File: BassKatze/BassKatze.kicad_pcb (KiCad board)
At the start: 2 copper layers, 55 x 54.9 mm, 55 parts, among them J1 Conn_01x02_Female, Q1 IRF7404, Q2 BSS138, Q3 BSS138, Q4 BSS138, Q5 BSS138, Q6 BSS138, SW1 SW_Push, U1 ATmega328-AU, U2 MSGEQ7, U3 TP4056

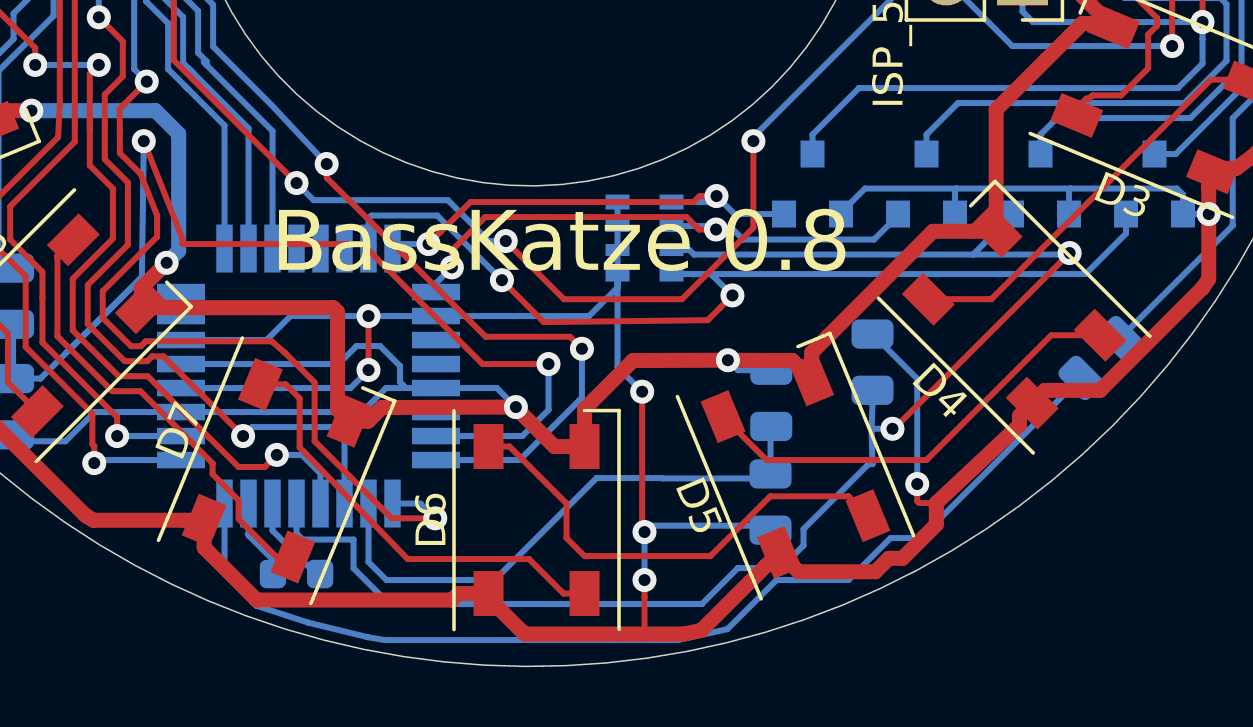
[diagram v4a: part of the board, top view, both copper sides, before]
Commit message: basskatze 0.9 -> removed redundant reset pullup
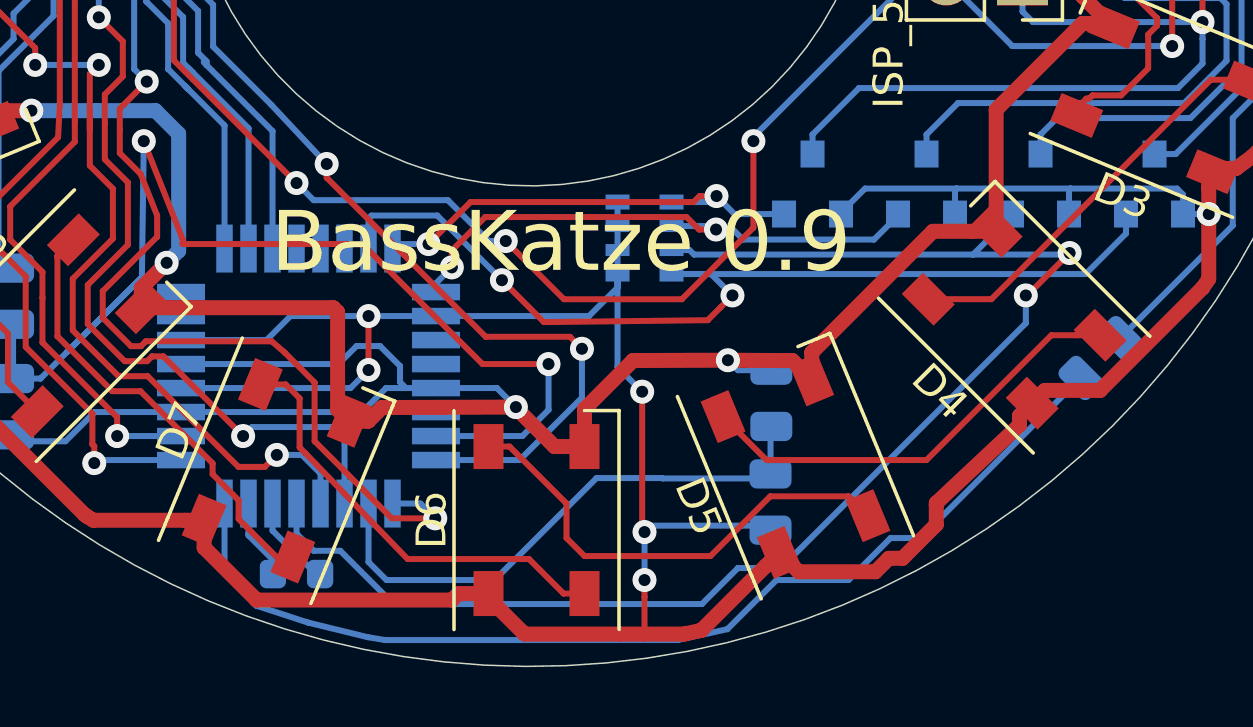
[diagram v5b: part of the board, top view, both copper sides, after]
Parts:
- removed R5: 10KOhm, Resistor_SMD:R_0805_2012Metric
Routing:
- net PWR: track 282.6 -> 275.8 mm, vias 14 -> 13
- net Reset: track 50.7 -> 48.4 mm
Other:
- board text added: "BassKatze 0.9"
- board text removed: "BassKatze 0.8"
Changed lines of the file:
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@@
     (thickness 1.6)
     (drawings 5)
-    (tracks 1097)
+    (tracks 1084)
     (zones 0)
-    (modules 55)
+    (modules 54)
     (nets 56)
   )
@@
     )
   )
-  (module Resistor_SMD:R_0805_2012Metric (layer B.Cu)
-    (at 138.4 144.3375 90)
-    (descr "Resistor SMD 0805 (2012 Metric), square (rectangular) end terminal, IPC_7351 nominal, (Body size source: https://docs.google.com/spreadsheets/d/1BsfQQcO9C6DZCsRaXUlFlo91Tg2WpOkGARC1WS5S8t0/edit?usp=sharing), generated with kicad-footprint-generator")
-    (tags resistor)
-    (attr smd)
-    (fp_text reference R5 (at 0 1.65 90) (layer B.SilkS)
-      (effects (font (size 1 1) (thickness 0.15)) (justify mirror))
-    )
-    (fp_text value 10KOhm (at 0 -1.65 90) (layer B.Fab)
-      (effects (font (size 1 1) (thickness 0.15)) (justify mirror))
-    )
-    (fp_line (start -1 -0.6) (end -1 0.6) (layer B.Fab) (width 0.1))
-    (fp_line (start -1 0.6) (end 1 0.6) (layer B.Fab) (width 0.1))
-    (fp_line (start 1 0.6) (end 1 -0.6) (layer B.Fab) (width 0.1))
-    (fp_line (start 1 -0.6) (end -1 -0.6) (layer B.Fab) (width 0.1))
-    (fp_line (start -0.258578 0.71) (end 0.258578 0.71) (layer B.SilkS) (width 0.12))
-    (fp_line (start -0.258578 -0.71) (end 0.258578 -0.71) (layer B.SilkS) (width 0.12))
-    (fp_line (start -1.68 -0.95) (end -1.68 0.95) (layer B.CrtYd) (width 0.05))
-    (fp_line (start -1.68 0.95) (end 1.68 0.95) (layer B.CrtYd) (width 0.05))
-    (fp_line (start 1.68 0.95) (end 1.68 -0.95) (layer B.CrtYd) (width 0.05))
-    (fp_line (start 1.68 -0.95) (end -1.68 -0.95) (layer B.CrtYd) (width 0.05))
-    (fp_text user %R (at 0 0 90) (layer B.Fab)
-      (effects (font (size 0.5 0.5) (thickness 0.08)) (justify mirror))
-    )
-    (pad 1 smd roundrect (at -0.9375 0 90) (size 0.975 1.4) (layers B.Cu B.Paste B.Mask) (roundrect_rratio 0.25)
-      (net 10 Reset))
-    (pad 2 smd roundrect (at 0.9375 0 90) (size 0.975 1.4) (layers B.Cu B.Paste B.Mask) (roundrect_rratio 0.25)
-      (net 7 PWR))
-    (model ${KISYS3DMOD}/Resistor_SMD.3dshapes/R_0805_2012Metric.wrl
-      (at (xyz 0 0 0))
-      (scale (xyz 1 1 1))
-      (rotate (xyz 0 0 0))
-    )
-  )
   (module Resistor_SMD:R_1206_3216Metric_Pad1.42x1.75mm_HandSolder (layer B.Cu)
     (at 127.8255 112.8395 90)
@@
     )
   )
-  (gr_text "BassKatze 0.8" (at 128.016 140.335) (layer F.SilkS)
+  (gr_text "BassKatze 0.9" (at 128.016 140.335) (layer F.SilkS)
     (effects (font (size 2 2) (thickness 0.15)))
   )
@@
   (segment (start 147.1 114.895) (end 147.609654 114.895) (width 0.5) (layer B.Cu) (net 7))
   (via (at 149.2 113.304654) (size 0.8) (drill 0.4) (layers F.Cu B.Cu) (net 7))
-  (via (at 139.889844 148.4) (size 0.8) (drill 0.4) (layers F.Cu B.Cu) (net 7))
-  (segment (start 138.4 143.4) (end 139.889844 144.889844) (width 0.2) (layer B.Cu) (net 7))
-  (segment (start 139.889844 144.889844) (end 139.889844 148.4) (width 0.2) (layer B.Cu) (net 7))
-  (segment (start 139.889844 148.965685) (end 139.958659 149.0345) (width 0.2) (layer F.Cu) (net 7))
-  (segment (start 139.889844 148.4) (end 139.889844 148.965685) (width 0.2) (layer F.Cu) (net 7))
-  (segment (start 139.958659 149.0345) (end 140.5255 149.0345) (width 0.2) (layer F.Cu) (net 7))
   (segment (start 140.5255 149.0345) (end 143.298813 146.433095) (width 0.5) (layer F.Cu) (net 7))
   (segment (start 101.95 125.6) (end 101.7 125.6) (width 0.5) (layer F.Cu) (net 7))
@@
   (segment (start 133.331001 142.512999) (end 132.9055 142.9385) (width 0.2) (layer F.Cu) (net 9))
   (segment (start 127.4445 143.002) (end 132.9055 142.9385) (width 0.2) (layer F.Cu) (net 9))
-  (segment (start 107.315 123.444) (end 107.188 123.571) (width 0.2) (layer B.Cu) (net 17))
-  (segment (start 138.4 145.7625) (end 138.4 145.275) (width 0.2) (layer B.Cu) (net 10))
-  (segment (start 122.292881 152.400001) (end 132.712459 152.400001) (width 0.2) (layer B.Cu) (net 10))
-  (segment (start 121.09999 151.20711) (end 122.292881 152.400001) (width 0.2) (layer B.Cu) (net 10))
-  (segment (start 121.09999 150.250001) (end 121.09999 151.20711) (width 0.2) (layer B.Cu) (net 10))
-  (segment (start 119.404999 150.250001) (end 121.09999 150.250001) (width 0.2) (layer B.Cu) (net 10))
-  (segment (start 119.2 150.045002) (end 119.404999 150.250001) (width 0.2) (layer B.Cu) (net 10))
-  (segment (start 119.2 149.05) (end 119.2 150.045002) (width 0.2) (layer B.Cu) (net 10))
   (segment (start 132.3 140.6) (end 131.7 140.6) (width 0.2) (layer B.Cu) (net 10))
   (segment (start 132.450011 140.750011) (end 132.3 140.6) (width 0.2) (layer B.Cu) (net 10))
@@
   (segment (start 143.05 139.45) (end 141.749989 140.750011) (width 0.2) (layer B.Cu) (net 10))
   (segment (start 143.05 139.4) (end 143.05 139.45) (width 0.2) (layer B.Cu) (net 10))
+  (segment (start 144.920489 140.750011) (end 144.9705 140.7) (width 0.2) (layer B.Cu) (net 10))
+  (segment (start 141.749989 140.750011) (end 144.920489 140.750011) (width 0.2) (layer B.Cu) (net 10))
   (via (at 144.9705 140.7) (size 0.8) (drill 0.4) (layers F.Cu B.Cu) (net 10))
-  (segment (start 141.749989 140.750011) (end 144.920489 140.750011) (width 0.2) (layer B.Cu) (net 10))
-  (segment (start 144.920489 140.750011) (end 144.9705 140.7) (width 0.2) (layer B.Cu) (net 10))
-  (via (at 139.065 146.558) (size 0.8) (drill 0.4) (layers F.Cu B.Cu) (net 10))
-  (segment (start 144.9705 140.7) (end 139.1125 146.558) (width 0.2) (layer F.Cu) (net 10))
-  (segment (start 139.1125 146.558) (end 139.065 146.558) (width 0.2) (layer F.Cu) (net 10))
-  (segment (start 138.4 147.73756) (end 138.3665 146.558) (width 0.2) (layer B.Cu) (net 10))
-  (segment (start 139.065 146.558) (end 138.3665 146.558) (width 0.2) (layer B.Cu) (net 10))
-  (segment (start 138.3665 146.558) (end 138.4 145.7625) (width 0.2) (layer B.Cu) (net 10))
-  (segment (start 136.10001 150.447906) (end 135.347926 151.19999) (width 0.2) (layer B.Cu) (net 10))
-  (segment (start 133.91247 151.19999) (end 132.712459 152.400001) (width 0.2) (layer B.Cu) (net 10))
-  (segment (start 135.347926 151.19999) (end 133.91247 151.19999) (width 0.2) (layer B.Cu) (net 10))
-  (segment (start 136.10001 149.90399) (end 136.10001 150.447906) (width 0.2) (layer B.Cu) (net 10))
-  (segment (start 138.26644 147.73756) (end 136.10001 149.90399) (width 0.2) (layer B.Cu) (net 10))
-  (segment (start 138.4 147.73756) (end 138.26644 147.73756) (width 0.2) (layer B.Cu) (net 10))
+  (via (at 143.51 142.113) (size 0.8) (drill 0.4) (layers F.Cu B.Cu) (net 10))
+  (segment (start 144.9705 140.7) (end 143.5575 142.113) (width 0.2) (layer F.Cu) (net 10))
+  (segment (start 143.5575 142.113) (end 143.51 142.113) (width 0.2) (layer F.Cu) (net 10))
+  (segment (start 143.51 143.037916) (end 143.51 142.113) (width 0.2) (layer B.Cu) (net 10))
+  (segment (start 135.347926 151.19999) (end 143.51 143.037916) (width 0.2) (layer B.Cu) (net 10))
+  (segment (start 133.91247 151.19999) (end 135.347926 151.19999) (width 0.2) (layer B.Cu) (net 10))
+  (segment (start 132.712459 152.400001) (end 133.91247 151.19999) (width 0.2) (layer B.Cu) (net 10))
+  (segment (start 122.434302 152.4) (end 132.712459 152.400001) (width 0.2) (layer B.Cu) (net 10))
+  (segment (start 119.77499 150.62499) (end 120.659292 150.62499) (width 0.2) (layer B.Cu) (net 10))
+  (segment (start 120.659292 150.62499) (end 122.434302 152.4) (width 0.2) (layer B.Cu) (net 10))
+  (segment (start 119.2 150.05) (end 119.77499 150.62499) (width 0.2) (layer B.Cu) (net 10))
+  (segment (start 119.2 149.05) (end 119.2 150.05) (width 0.2) (layer B.Cu) (net 10))
   (via (at 133.184316 139.915687) (size 0.8) (drill 0.4) (layers F.Cu B.Cu) (net 11))
   (segment (start 131.7 139.8) (end 133.068629 139.8) (width 0.2) (layer B.Cu) (net 11))
@@
   (segment (start 112.609469 131.377906) (end 112.609469 132.842) (width 0.2) (layer B.Cu) (net 16))
   (segment (start 109.601 123.6345) (end 109.6645 127.8255) (width 0.2) (layer B.Cu) (net 16))
+  (segment (start 107.315 123.444) (end 107.188 123.571) (width 0.2) (layer B.Cu) (net 17))
   (segment (start 109.267873 140.715373) (end 109.7534 141.2009) (width 0.2) (layer B.Cu) (net 17))
   (segment (start 108.650001 125.223501) (end 108.650001 127.798701) (width 0.2) (layer B.Cu) (net 17))

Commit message: basskatze 1.0 (fixed diode footprint, better manually solderable resistor arrays)
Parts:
- D1, D18, D19: footprint Diode_SMD:D_SOD-323 -> Diode_SMD:D_0805_2012Metric_Pad1.15x1.40mm_HandSolder
- RN1, RN2, RN3: footprint Resistor_SMD:R_Array_Convex_4x0603 -> Resistor_SMD:R_Array_Convex_4x1206
- moved D19 13.0 mm to (131.8, 102.1), turned to 270 degrees
- moved RN3 1.55 mm to (131.4, 141.6)
- moved RN2 1.12 mm to (143.0, 111.0)
- moved Q2 0.89 mm to (147.1, 112.0)
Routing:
- net 5V_Flash: track 106.2 -> 88.9 mm, vias 8 -> 3
- net MOSI_5V: track 34.7 -> 28.5 mm
- net LED1: track 26.2 -> 31.5 mm
- net MISO_5V: track 25.9 -> 21.2 mm, vias 2 -> 1
- net SCK_5V: track 25.9 -> 27.8 mm
- net MISO: track 15.6 -> 17.4 mm
- net Net-(D2-Pad4): track 17.0 -> 15.4 mm
- net PWR: track 275.8 -> 277.0 mm
- net MOSI: track 33.7 -> 32.5 mm
- net Net-(D18-Pad1): track 22.5 -> 21.4 mm
- net Net-(Q1-Pad4): track 2.49 -> 3.34 mm
- net Reset: track 48.4 -> 47.7 mm
- net Net-(Q2-Pad1): track 4.52 -> 5.19 mm
- net BAT+: track 23.2 -> 23.8 mm
- net Reset_5V: track 24.1 -> 23.8 mm, vias 1 -> 0
- added copper zone on B.Cu, net BAT-
- added copper zone on F.Cu, net BAT-
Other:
- board text added: "BassKatze 1.0"
- board text removed: "BassKatze 0.9"
